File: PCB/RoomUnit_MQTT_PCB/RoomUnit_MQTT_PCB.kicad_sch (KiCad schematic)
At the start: 26 parts, among them J1 Conn_01x08_Socket, Q1 MMBTA06, U1 LMV393, U2 MOUDLE-SEEEDUINO-XIAO-ESP32C3, U3 L78L24_SOT89

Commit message: pcb progress
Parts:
- removed J1: Conn_01x08_Socket, Connector_Samtec_HPM_THT:Samtec_HPM-08-01-x-S_Straight_1x08_Pitch5.08mm, symbol Connector:Conn_01x08_Socket
- removed R4, R7: 18k, Resistor_SMD:R_0805_2012Metric_Pad1.20x1.40mm_HandSolder, symbol Device:R
- removed U2: MOUDLE-SEEEDUINO-XIAO-ESP32C3, RF_Module:MCU_Seeed_ESP32C3, symbol Seeed studio:MOUDLE-SEEEDUINO-XIAO-ESP32C3
- added J1, J2: Conn_01x07_Socket, Project_Library:XIAO_ESP32-C3_Custom_Connector, symbol Connector:Conn_01x07_Socket
- added U4: ~, Project_Library:RoomUnit_Connector_5mm, symbol Project_Library:RoomUnit_Connector
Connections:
- net +24V: now also U4.2 (VCC)
- net +3V3: now also J2.3 (Pin_3)
- net +5V: now also J2.1 (Pin_1)
- net AO1: now also U4.6 (AO1)
- net AO2: now also U4.7 (AO2)
- net AO3: now also U4.8 (AO3)
- net GND: now also J2.2 (Pin_2), U4.1 (GND), U4.4 (GND)
- net MPS: now also U4.3 (MPS)
- net at R10.2: now also J1.1 (Pin_1)
- net at R12.2: now also J1.3 (Pin_3)
- net at R11.2: now also J1.2 (Pin_2)
- net at R13.2: now also J1.7 (Pin_7)
- net at R14.1: now also J2.7 (Pin_7)
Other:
- moved on the sheet: C2, D1, D2, L1, Q1, R10, R11, R12, R13, R14, R8, R9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

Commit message: applied schematic changes (wip)
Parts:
- removed D1: BAS40-04, Package_TO_SOT_SMD:SOT-23, symbol Diode:BAS40-04
- removed D2: D, Diode_SMD:D_0805_2012Metric, symbol Device:D
- removed U3: L78L24_SOT89, Package_TO_SOT_SMD:SOT-89-3, symbol Regulator_Linear:L78L24_SOT89
- added R15: 33k, Resistor_SMD:R_0805_2012Metric_Pad1.20x1.40mm_HandSolder, symbol Device:R
- added R16: 1k, Resistor_SMD:R_0805_2012Metric_Pad1.20x1.40mm_HandSolder, symbol Device:R
- added R4: 4.7k, Resistor_SMD:R_0805_2012Metric_Pad1.20x1.40mm_HandSolder, symbol Device:R
- added R7: 1M, Resistor_SMD:R_0805_2012Metric_Pad1.20x1.40mm_HandSolder, symbol Device:R
- added U2: TLV61046ADB, Package_TO_SOT_SMD:SOT-23-6, symbol Regulator_Switching:TLV61046ADB
- C3: value 330n -> 1u; footprint Capacitor_SMD:C_0805_2012Metric_Pad1.18x1.45mm_HandSolder -> (none)
- C4: value 100n -> 4.7u; footprint Capacitor_SMD:C_0805_2012Metric_Pad1.18x1.45mm_HandSolder -> (none)
- L1: value L -> 10u; footprint Inductor_SMD:L_Ferrocore_DLG-0705 -> Inductor_SMD:L_APV_APH0420
- R2: value 690k -> 680k
- R6: value 9.2k -> 8.2k
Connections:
- net +24V: now also R7.1, U2.5 (VOUT)
- net +3V3: now also R4.1
- net +5V: now also L1.1, U2.4 (EN), U2.6 (VI)
- net AO1: now also U4.5 (AO1); no longer U4.6 (AO1)
- net AO2: now also U4.6 (AO2); no longer U4.7 (AO2)
- net AO3: now also U4.7 (AO3); no longer U4.8 (AO3)
- net GND: now also R16.2, U2.2 (GND)
- net MPS: now also Q1.3 (C), R4.2
- net at L1.2: now also U2.1 (SW); no longer Q1.3 (C)
- new net: R15.1, R7.2, U2.3 (FB)
- new net: R15.2, R16.1
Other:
- moved on the sheet: C1, C4, U1C

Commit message: PCB improvements
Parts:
- C3, C4: footprint (none) -> Capacitor_SMD:C_1206_3216Metric
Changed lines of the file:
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@@
 			)
 		)
-		(property "Footprint" ""
+		(property "Footprint" "Capacitor_SMD:C_1206_3216Metric"
 			(at 262.5852 120.65 0)
 			(effects
@@
 			)
 		)
-		(property "Footprint" ""
+		(property "Footprint" "Capacitor_SMD:C_1206_3216Metric"
 			(at 216.8652 118.11 0)
 			(effects

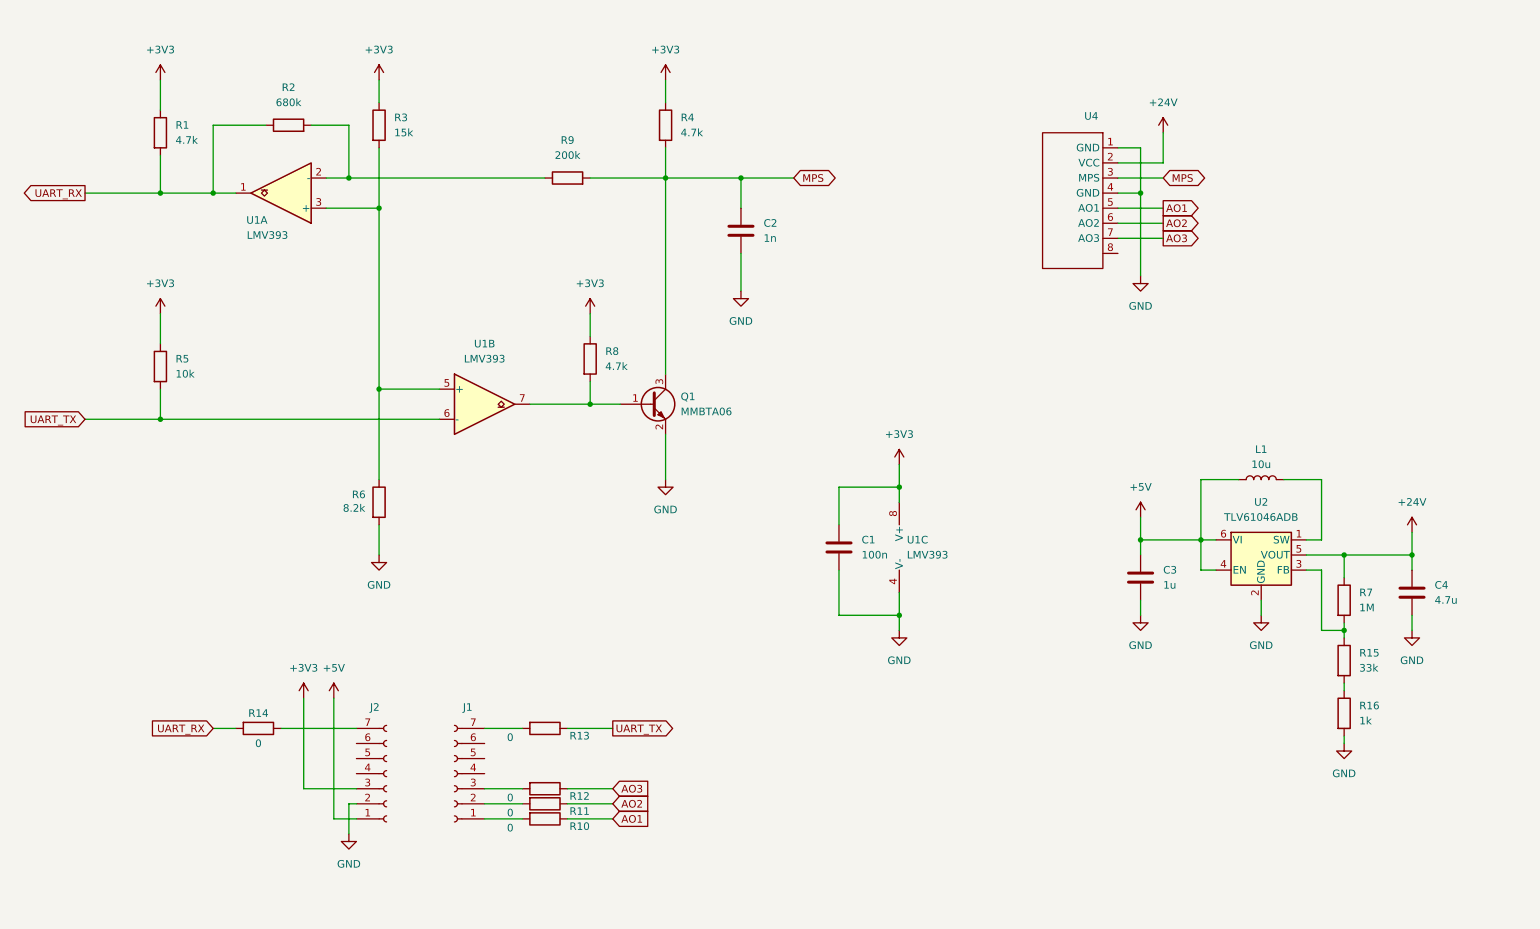
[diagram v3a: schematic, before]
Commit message: schematic updated 18V
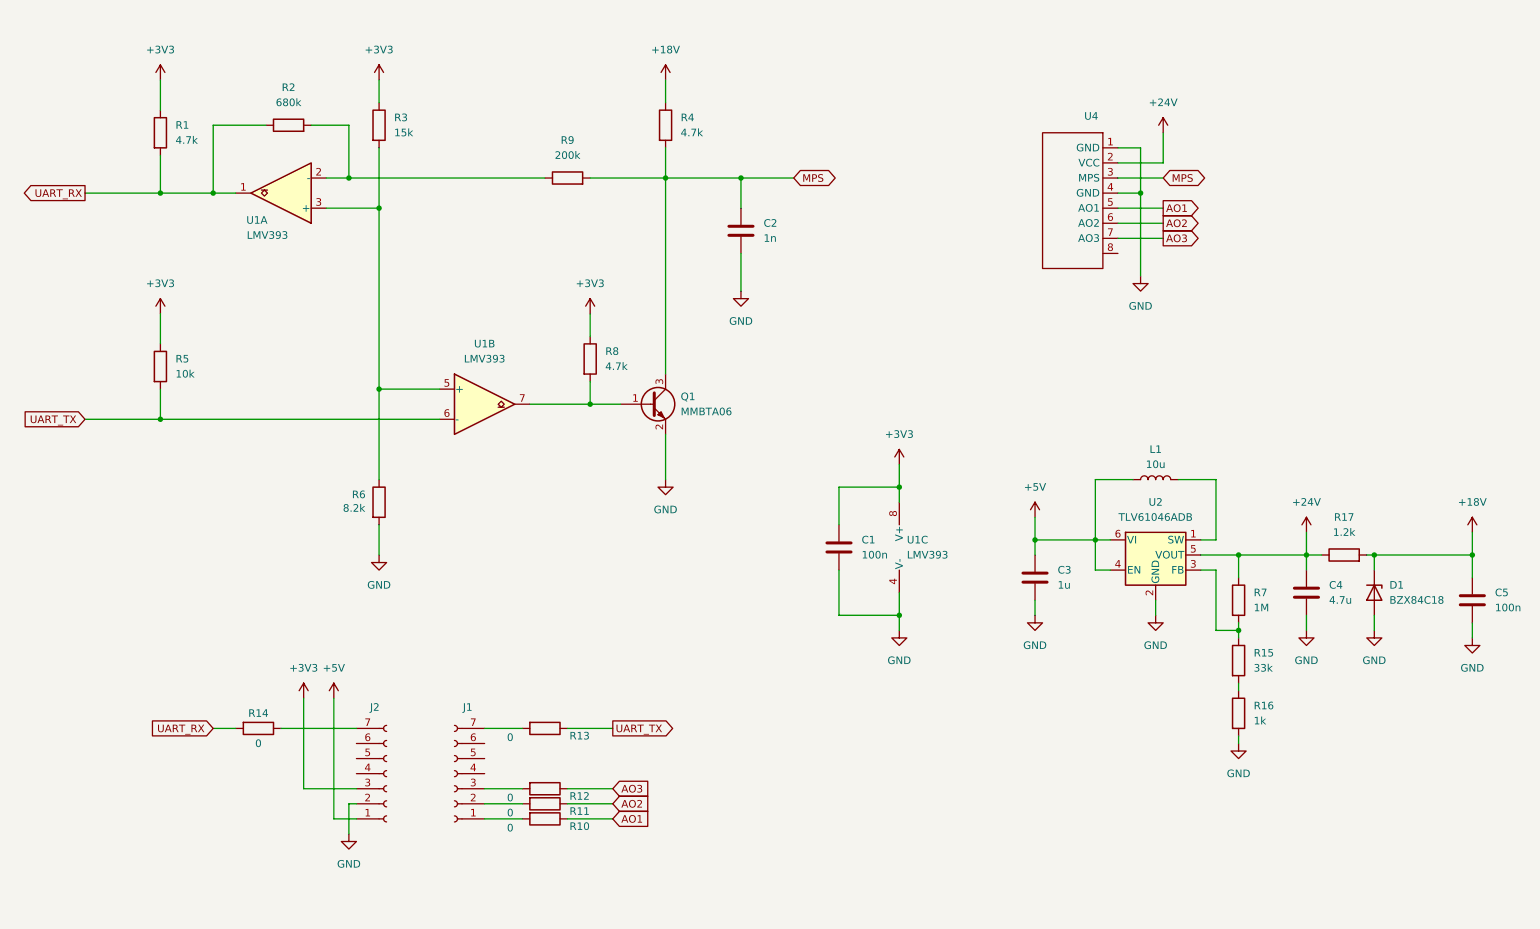
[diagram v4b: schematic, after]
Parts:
- added C5: 100n, Capacitor_SMD:C_0805_2012Metric_Pad1.18x1.45mm_HandSolder, symbol Device:C
- added D1: BZX84C18, Package_TO_SOT_SMD:SOT-23, symbol Diode:BZX84Cxx
- added R17: 1.2k, Resistor_SMD:R_0805_2012Metric_Pad1.20x1.40mm_HandSolder, symbol Device:R
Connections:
- net +24V: now also R17.1
- net +3V3: no longer R4.1
- net GND: now also C5.2, D1.1 (A)
- new net +18V: C5.1, D1.3 (K), R17.2, R4.1
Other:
- moved on the sheet: C3, C4, L1, R15, R16, R7, U2

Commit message: SChematic update - PCB almost done
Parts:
- R16: value 1k -> 1.6k
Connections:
- net at R2.2, R9.1: now also U1.3 (+); no longer U1.2 (-)
- net at R3.2, R6.1, U1.5 (+): now also U1.2 (-); no longer U1.3 (+)
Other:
- moved on the sheet: U1A
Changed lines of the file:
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@@
 			)
 		)
-		(property "Value" "1k"
+		(property "Value" "1.6k"
 			(at 234.95 138.4299 0)
 			(effects
@@
 	(symbol
 		(lib_id "Comparator:LMV393")
-		(at 71.12 49.53 180)
+		(at 71.12 49.53 0)
+		(mirror y)
 		(unit 1)
 		(exclude_from_sim no)
@@
 		(dnp no)
 		(property "Reference" "U1"
-			(at 67.056 54.102 0)
+			(at 67.056 44.958 0)
 			(effects
 				(font
@@
 		)
 		(property "Value" "LMV393"
-			(at 68.834 56.642 0)
-			(effects
-				(font
+			(at 68.834 42.418 0)
+			(effects
+				(font

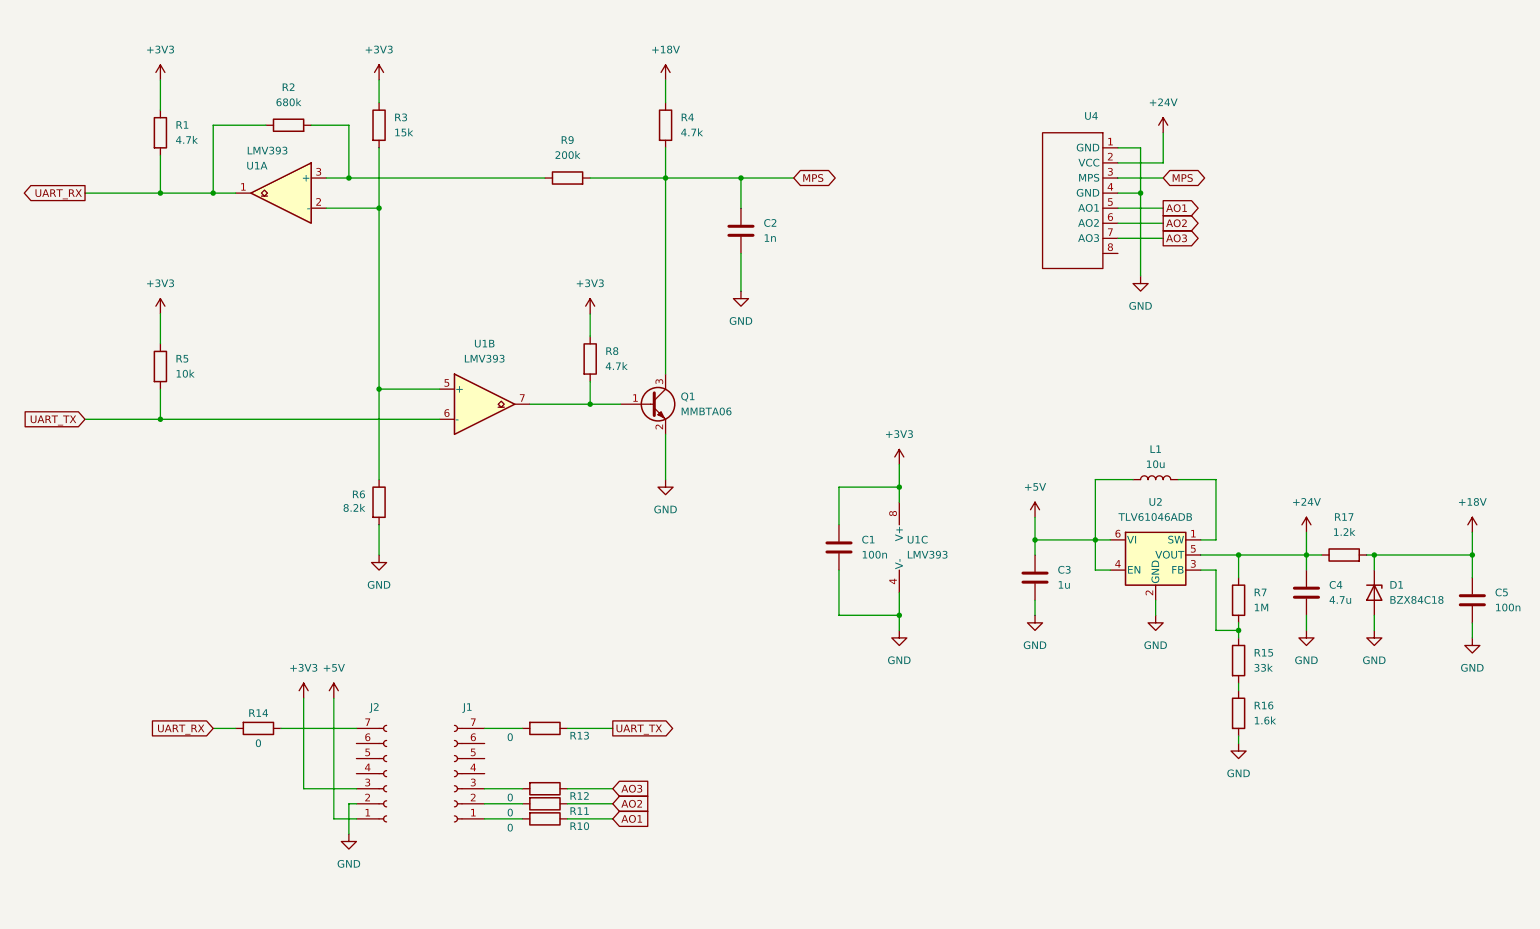
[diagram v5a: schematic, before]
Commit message: Spannungsteiler AOx
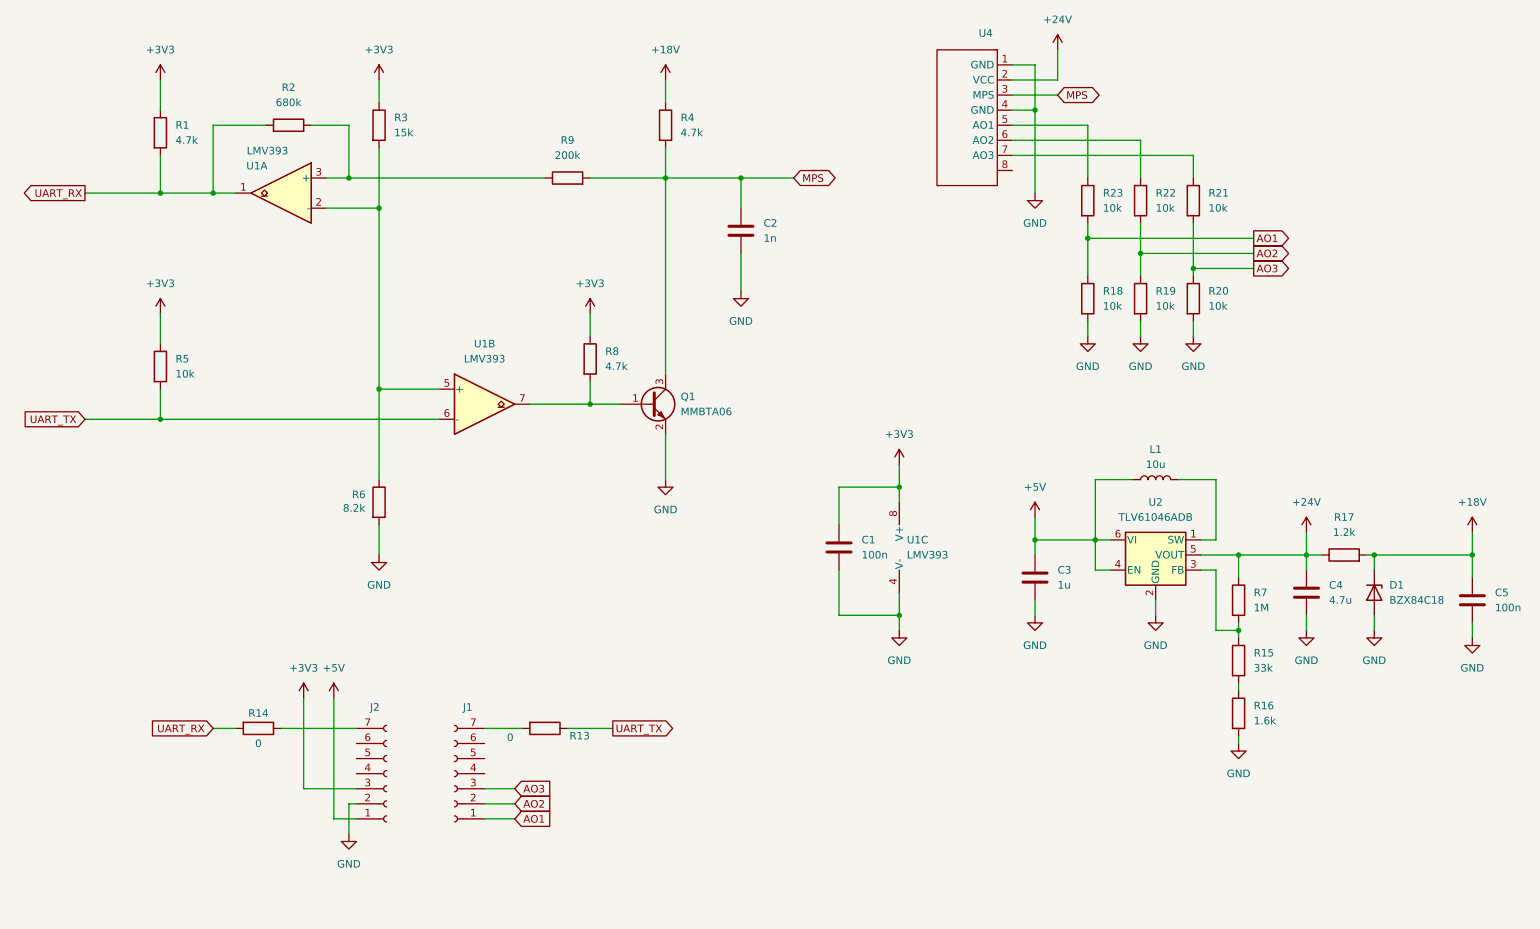
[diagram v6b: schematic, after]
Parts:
- removed R10, R11, R12: 0, Resistor_SMD:R_0805_2012Metric_Pad1.20x1.40mm_HandSolder, symbol Device:R
- added R18, R19, R20, R21, R22, R23: 10k, Resistor_SMD:R_0805_2012Metric_Pad1.20x1.40mm_HandSolder, symbol Device:R
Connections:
- net AO1: now also J1.1 (Pin_1), R18.1, R23.2; no longer U4.5 (AO1)
- net AO2: now also J1.2 (Pin_2), R19.1, R22.2; no longer U4.6 (AO2)
- net AO3: now also J1.3 (Pin_3), R20.1, R21.2; no longer U4.7 (AO3)
- net GND: now also R18.2, R19.2, R20.2
- new net: R21.1, U4.7 (AO3)
- new net: R23.1, U4.5 (AO1)
- new net: R22.1, U4.6 (AO2)
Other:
- moved on the sheet: U4

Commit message: fixed placement and package
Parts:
- L1: footprint Inductor_SMD:L_APV_APH0420 -> Inductor_SMD:L_Chilisin_BMRA00040420
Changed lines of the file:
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@@
 			)
 		)
-		(property "Footprint" "Inductor_SMD:L_APV_APH0420"
+		(property "Footprint" "Inductor_SMD:L_Chilisin_BMRA00040420"
 			(at 218.44 97.79 0)
 			(effects

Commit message: Ordered
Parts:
- R21, R22, R23: now left out of the parts list
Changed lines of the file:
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@@
 		(unit 1)
 		(exclude_from_sim no)
-		(in_bom yes)
+		(in_bom no)
 		(on_board yes)
 		(dnp no)
@@
 		(unit 1)
 		(exclude_from_sim no)
-		(in_bom yes)
+		(in_bom no)
 		(on_board yes)
 		(dnp no)
@@
 		(unit 1)
 		(exclude_from_sim no)
-		(in_bom yes)
-		(on_board yes)
-		(dnp no)
+		(in_bom no)
+		(on_board yes)
+		(dnp no)
